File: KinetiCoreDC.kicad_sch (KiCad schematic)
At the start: 18 parts, among them J1 Conn_ARM_SWD_TagConnect_TC203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, J7 B2B-XH-A, Q1 BSN20, Q2 BSN20, U1 STM32G070KBT6, U4 THVD1400D, U5 MCP1703Ax-330xxDB, U9 LTC4365TS8

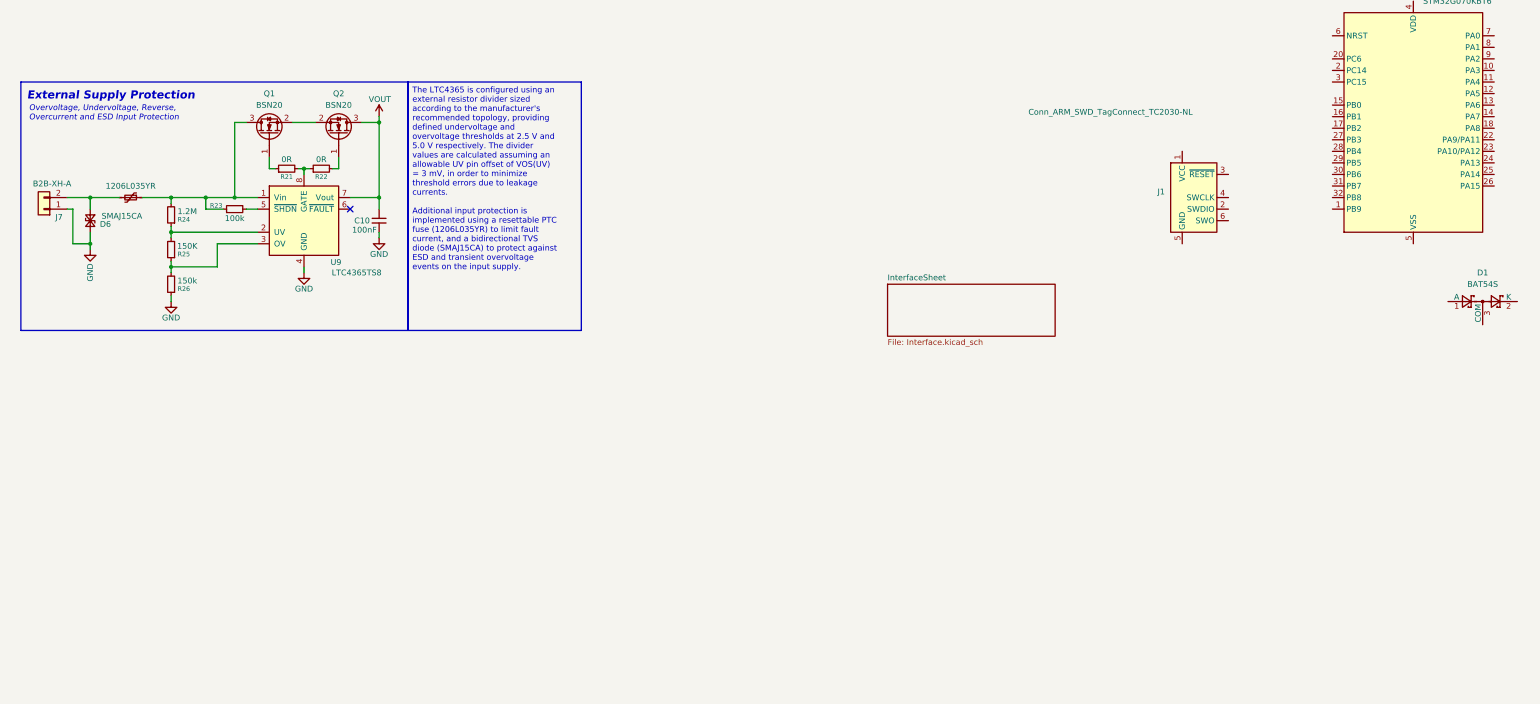
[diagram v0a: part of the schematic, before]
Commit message: git commit -m "Add RS485 transceiver circuitry"
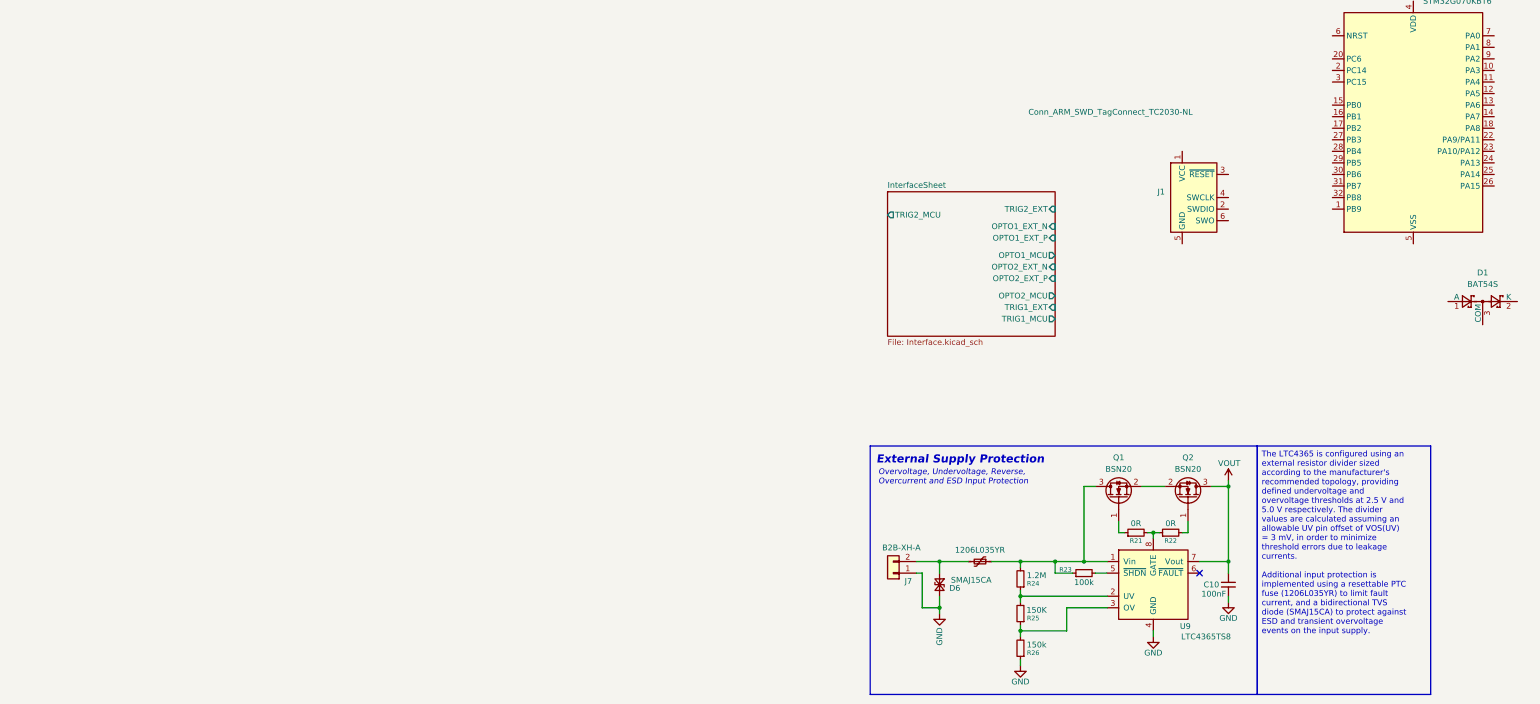
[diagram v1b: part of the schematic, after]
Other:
- sheet InterfaceSheet ports: added OPTO1_EXT_N, OPTO1_EXT_P, OPTO1_MCU, OPTO2_EXT_N, OPTO2_EXT_P, OPTO2_MCU, TRIG1_EXT, TRIG1_MCU, TRIG2_EXT, TRIG2_MCU; removed none
- moved on the sheet: C10, D6, J7, Q1, Q2, R21, R22, R23, R24, R25, R26, U9

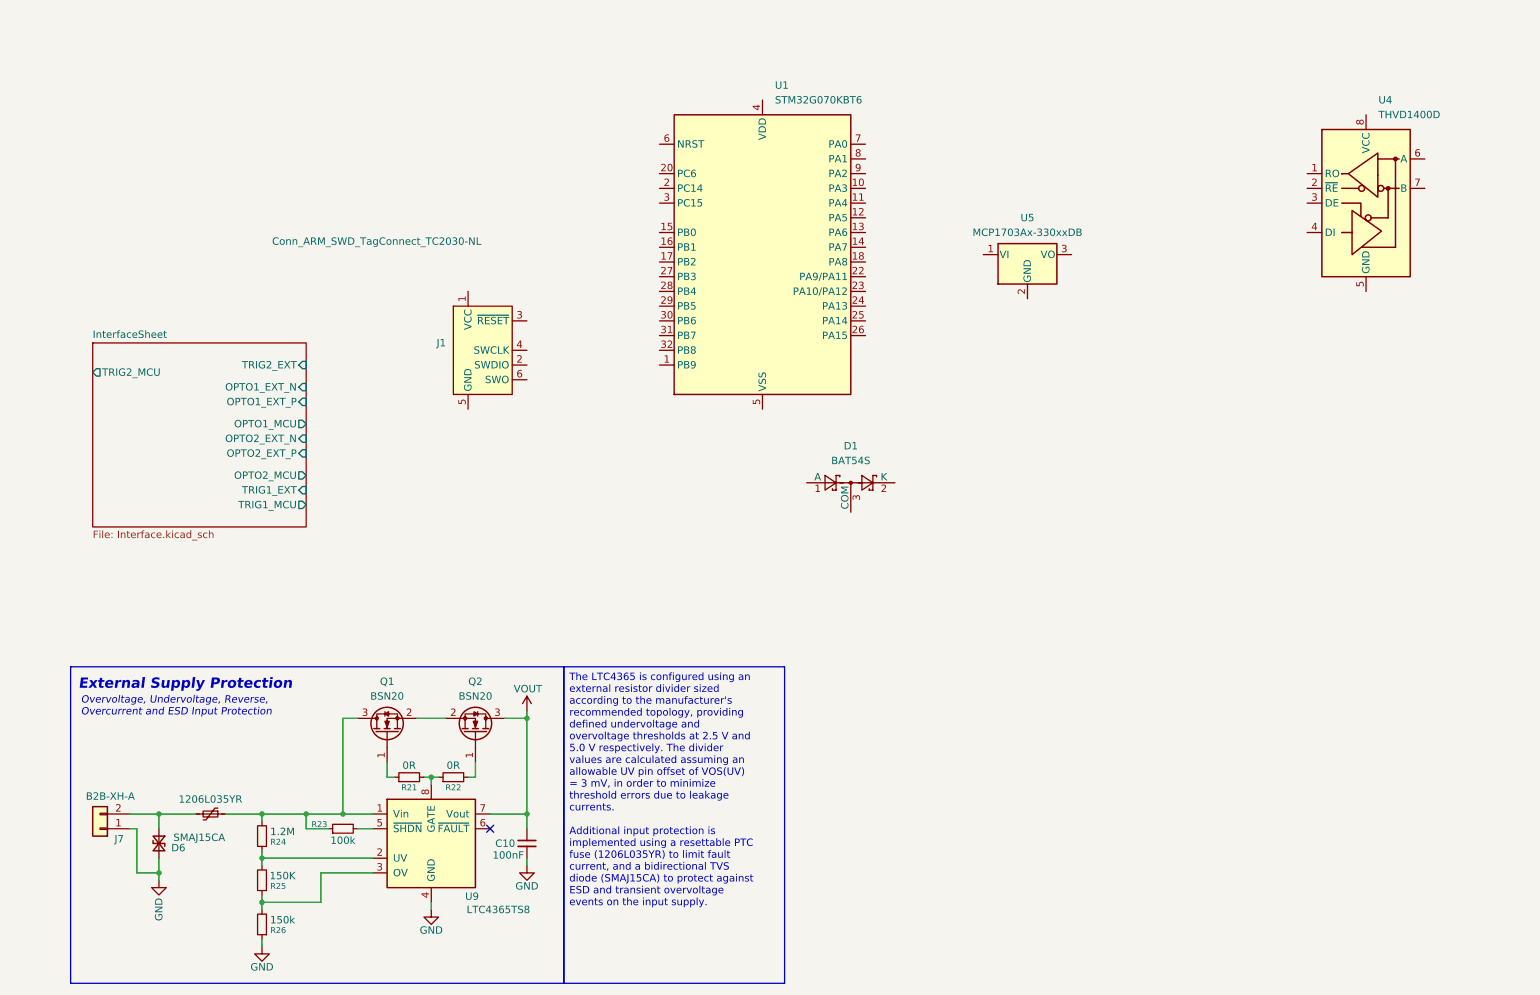
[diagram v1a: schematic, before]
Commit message: Update schematics: limit switches, debug TC2070 and power supply stage
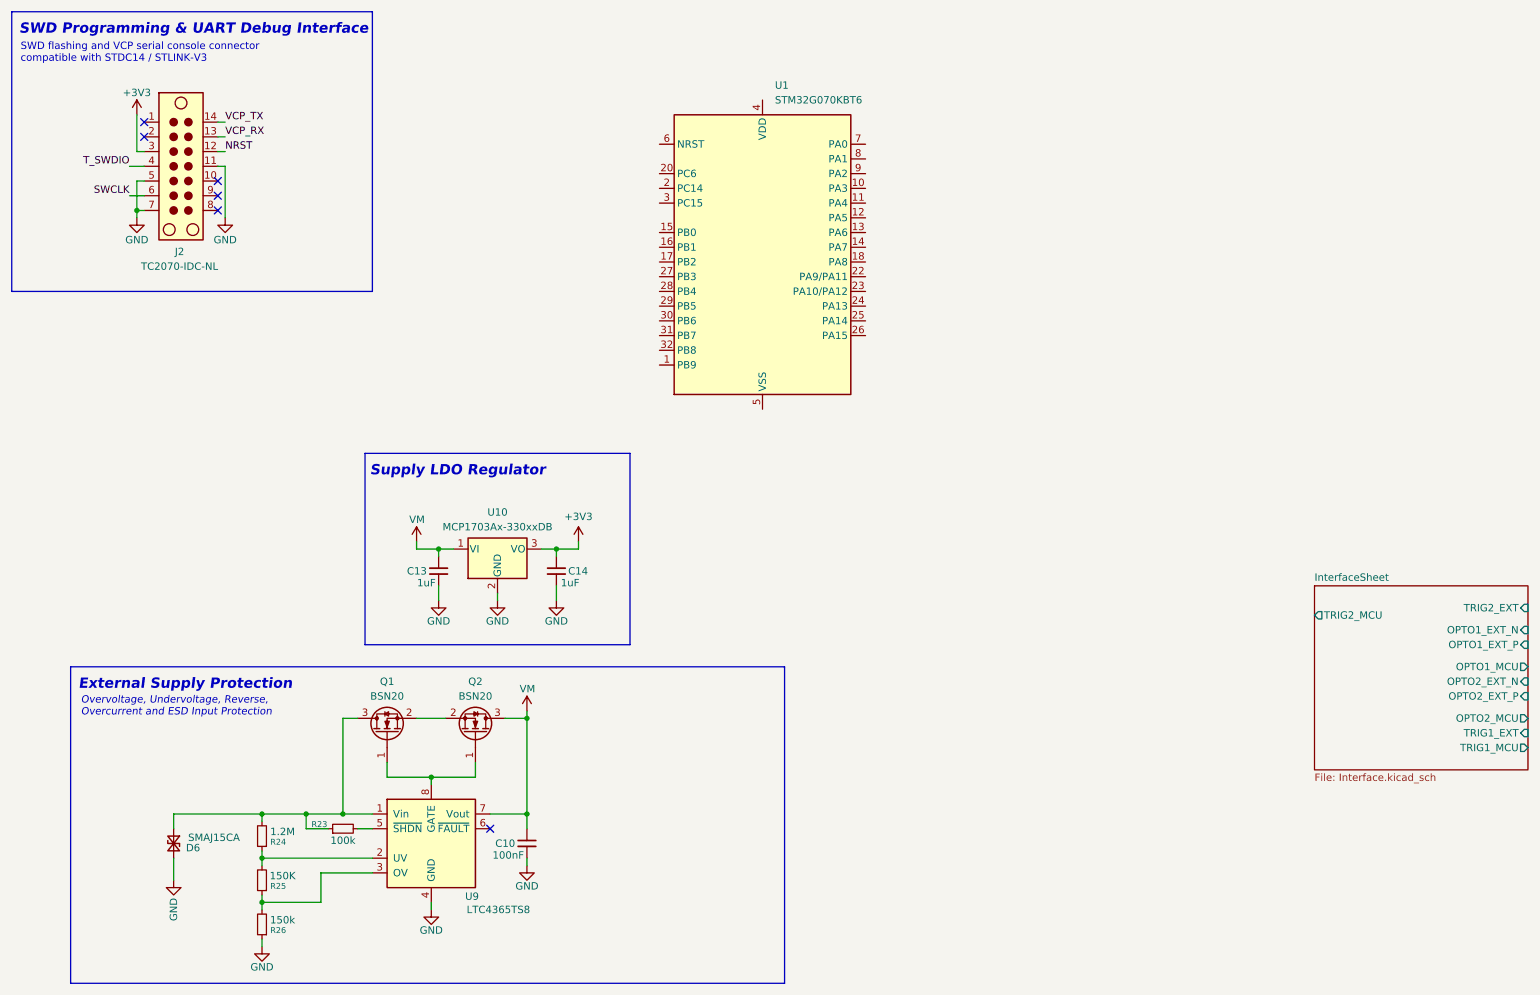
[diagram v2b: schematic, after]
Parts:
- removed 1206L035/16YR1: 1206L035YR, Fuse:Fuse_1206_3216Metric, symbol Device:Polyfuse_Small
- removed D1: BAT54S, Package_TO_SOT_SMD:SOT-23, symbol Diode:BAT54S
- removed J1: Conn_ARM_SWD_TagConnect_TC2030-NL, Connector:Tag-Connect_TC2030-IDC-NL_2x03_P1.27mm_Vertical, symbol Connector:Conn_ARM_SWD_TagConnect_TC2030-NL
- removed J7: B2B-XH-A, Connector_JST:JST_XH_B2B-XH-A_1x02_P2.50mm_Vertical, symbol Connector_Generic:Conn_01x02
- removed R21, R22: 0R, Resistor_SMD:R_0603_1608Metric, symbol Device:R_Small
- removed U4: THVD1400D, Package_SO:SOIC-8_3.9x4.9mm_P1.27mm, symbol Interface_UART:THVD1400D
- removed U5: MCP1703Ax-330xxDB, Package_TO_SOT_SMD:SOT-223-3_TabPin2, symbol Regulator_Linear:MCP1703Ax-330xxDB
- added C13, C14: 1uF, Capacitor_SMD:C_0603_1608Metric, symbol Device:C_Small
- added J2: TC2070-IDC-NL, Library:Tag-Connect_TC2070-IDC-FP_2x07_P1.27mm_Vertical, symbol Connector:TC2070
- added U10: MCP1703Ax-330xxDB, Package_TO_SOT_SMD:SOT-223-3_TabPin2, symbol Regulator_Linear:MCP1703Ax-330xxDB
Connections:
- net GND: now also C13.2, C14.2, J2.11, J2.5, J2.7, U10.2 (GND)
- net at Q1.3 (D), R23.1, R24.2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: now also D6.1 (A1)
- net at U9.8 (GATE): now also Q1.1 (G), Q2.1 (G)
- net VOUT renamed VM
- net VM: now also C13.1, U10.1 (VI)
- new net +3V3: C14.1, J2.3, U10.3 (VO)
- new net NRST: J2.12
- new net SWCLK: J2.6
- new net T_SWDIO: J2.4
- new net VCP_RX: J2.13
- new net VCP_TX: J2.14
- no-connect marks 1 -> 6
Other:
- note added: "SWD Programming & UART Debug Interface"
- note added: "SWD flashing and VCP serial console connector compatible with STDC14 / STLINK-V3"
- note added: "Supply LDO Regulator"
- moved on the sheet: D6

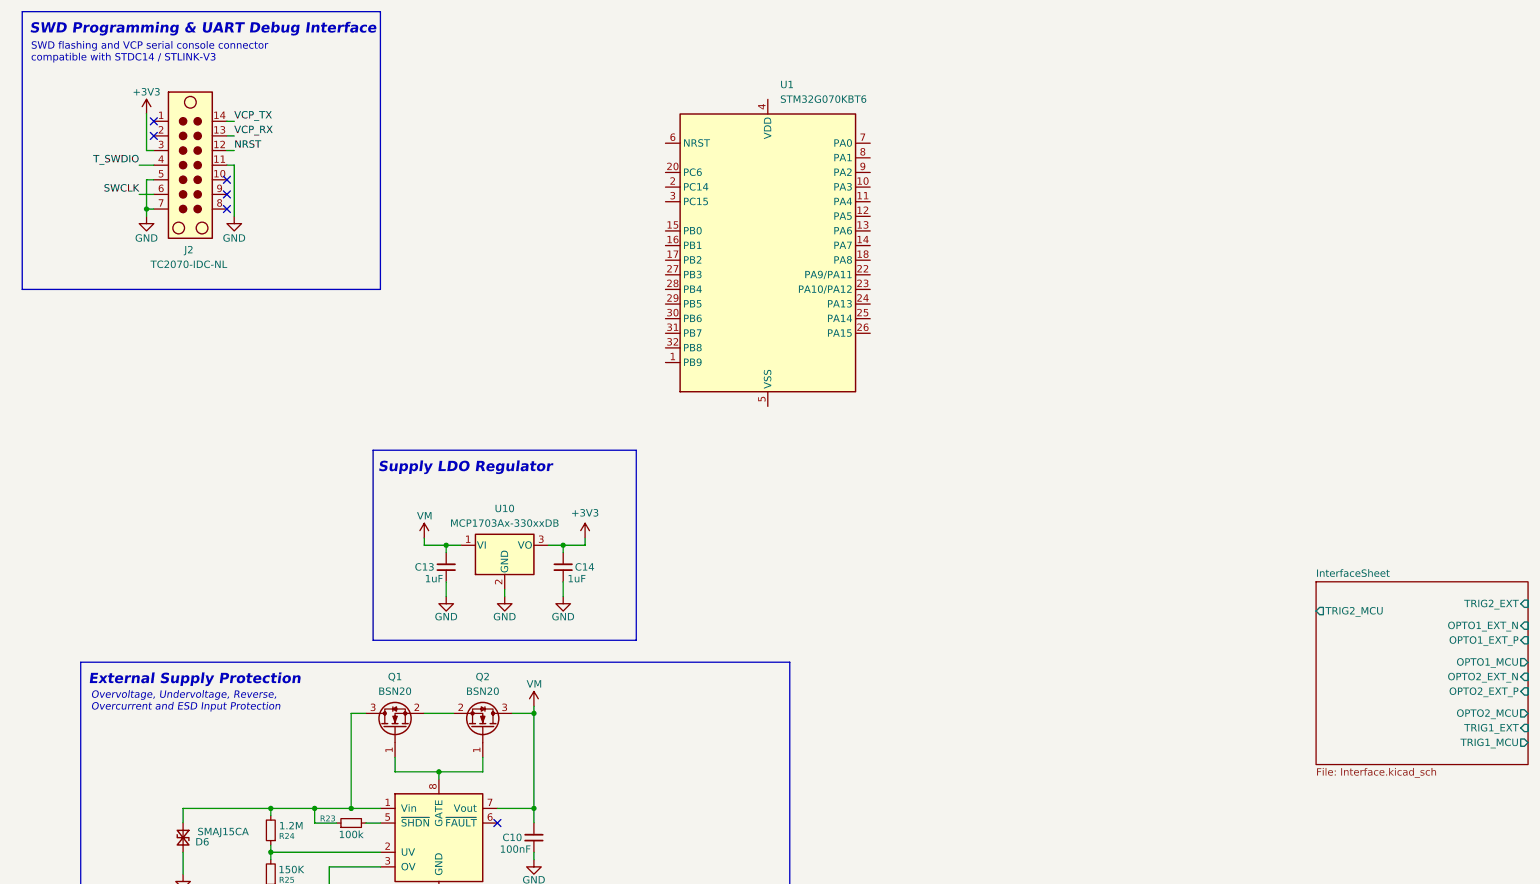
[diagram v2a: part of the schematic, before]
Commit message: feat(lib): initialize local project library and 3D step models
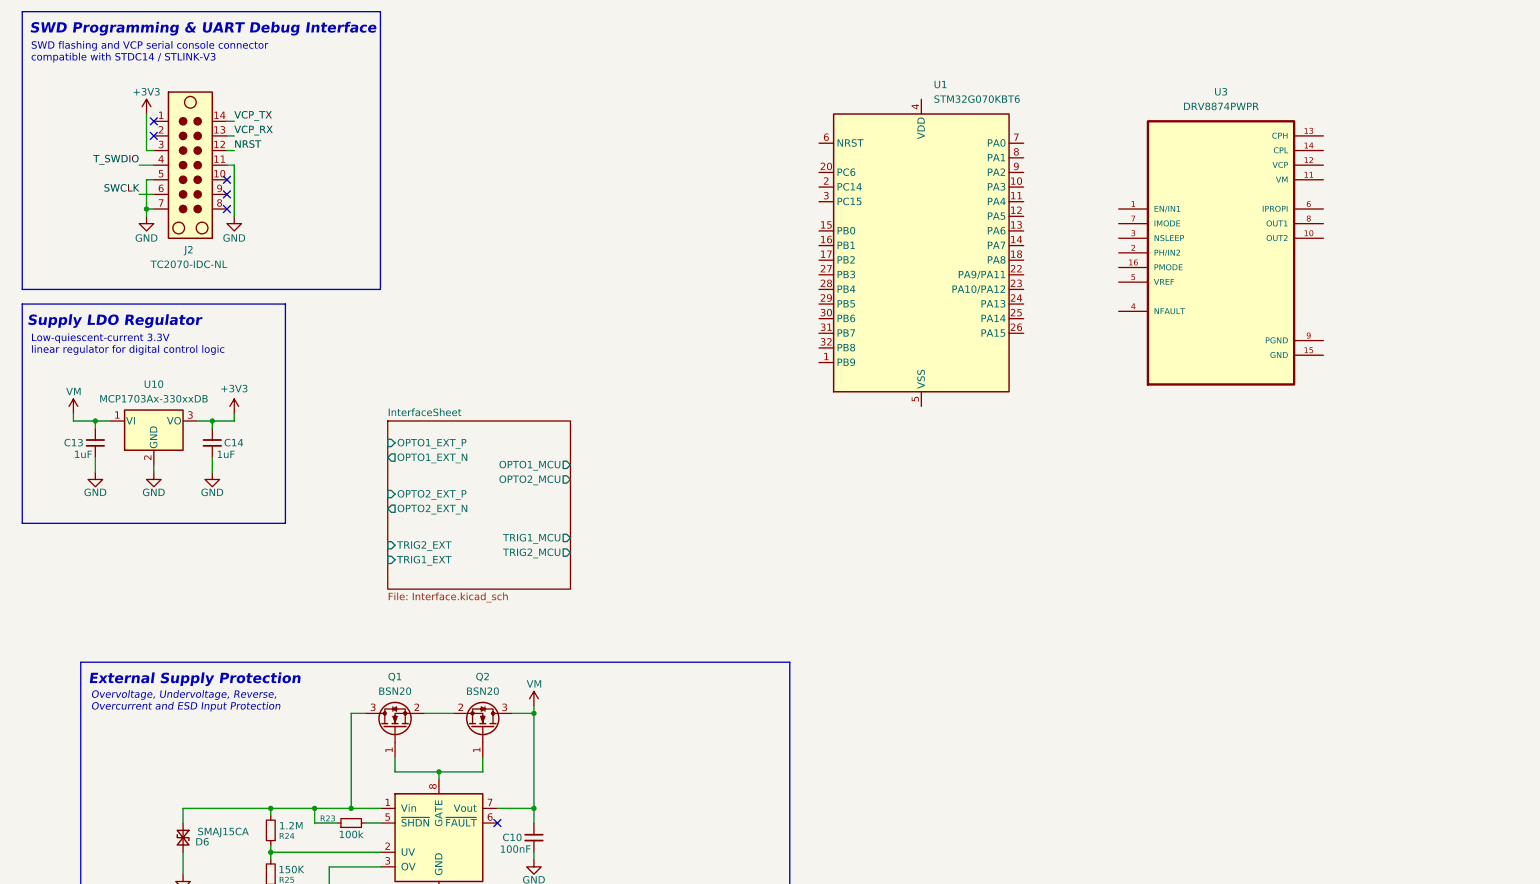
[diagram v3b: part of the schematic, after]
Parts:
- added U3: DRV8874PWPR, KineticCore:SOP65P640X120-17N, symbol KineticCore:DRV8874PWPR
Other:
- note added: "Low-quiescent-current 3.3V linear regulator for digital control logic"
- moved on the sheet: C13, C14, U1, U10
